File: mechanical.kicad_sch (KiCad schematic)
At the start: 9 parts

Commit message: Cleanup schematic
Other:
- note added: "Holes for studs"
- moved on the sheet: MP1, MP2, MP3, MP4, MP5, MP6, MP7, MP8, MP9

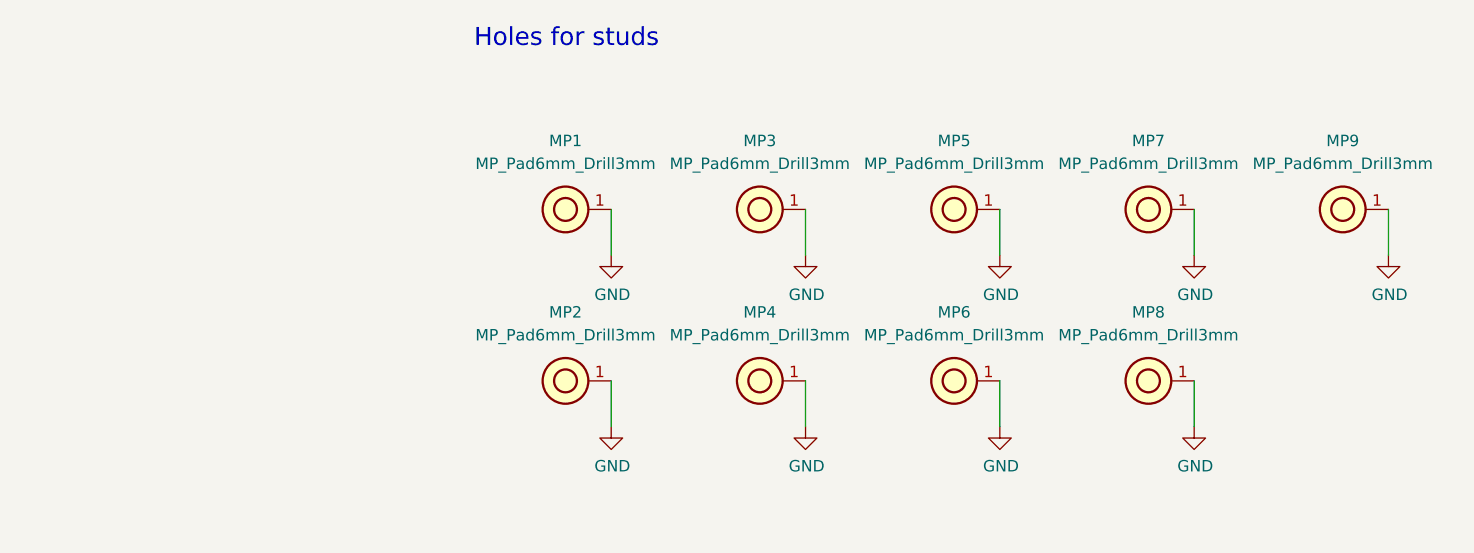
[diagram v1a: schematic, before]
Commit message: Replace old studs with new 10mm M2 model
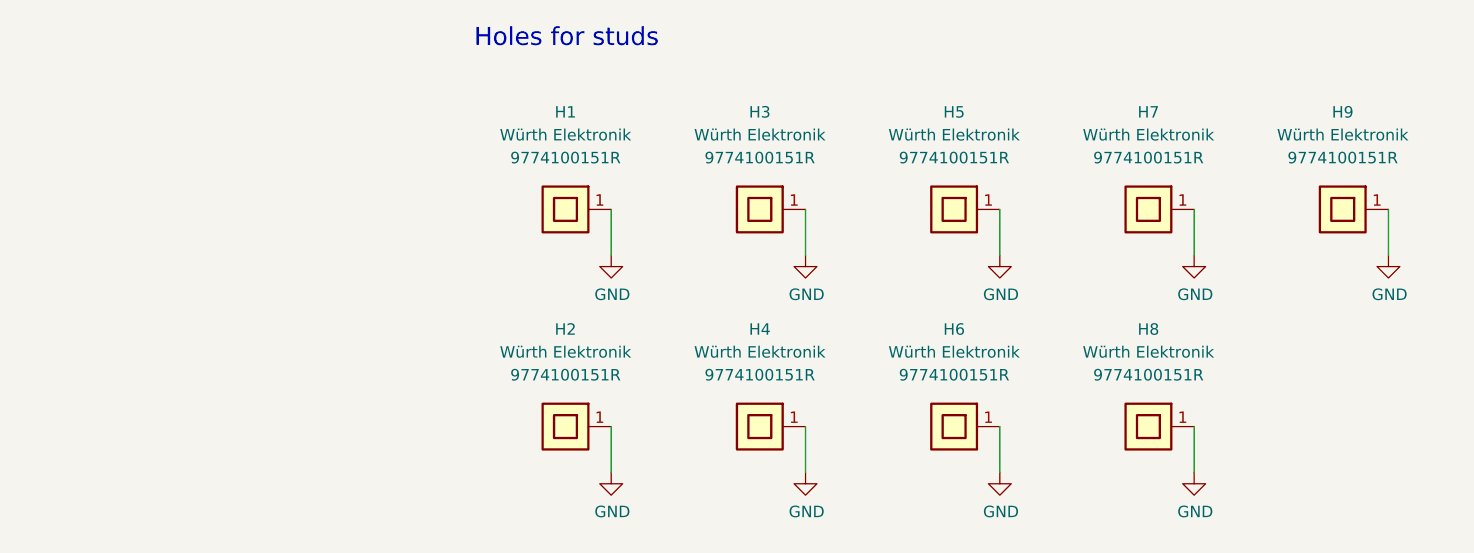
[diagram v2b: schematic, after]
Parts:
- removed MP1, MP2, MP3, MP4, MP5, MP6, MP7, MP8, MP9: MP_Pad6mm_Drill3mm, antmicro-footprints:MP_Pad6mm_Drill3mm, symbol antmicroMechanicalParts:MP_Pad6mm_Drill3mm
- added H1, H2, H3, H4, H5, H6, H7, H8, H9: Spacer_Drill3.7mm_H10mm_9774100151R, antmicro-footprints:Spacer_Drill3.7mm_H10mm_9774100151R, symbol antmicroMechanicalParts:Spacer_Drill3.7mm_H10mm_9774100151R
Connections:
- net GND: now also H1.1, H2.1, H3.1, H4.1, H5.1, H6.1, H7.1, H8.1, H9.1
